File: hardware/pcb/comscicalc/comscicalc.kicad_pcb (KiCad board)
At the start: 2 copper layers, 178.7 x 104.8 mm, 307 parts, among them IC1 TPS92360DCKR, IC2 AP62300TWU-7, IC3 FT811Q-T, IC4 TCA8418RTWR, J1 USB4110-GF-A, J2 TC2050-IDC, J3 4-1734839-0, SW1 SSSS211603, SW10 SW_Push, SW11 SW_Push, SW12 SW_Push, SW13 SW_Push, SW14 SW_Push, SW15 SW_Push, SW16 SW_Push, SW17 SW_Push, SW18 SW_Push, SW19 SW_Push, SW2 SW_Push, SW20 SW_Push, SW21 SW_Push, SW22 SW_Push, SW23 SW_Push, SW24 SW_Push, SW25 SW_Push, SW26 SW_Push, SW27 SW_Push, SW28 SW_Push, SW29 SW_Push, SW3 SW_Push, SW30 SW_Push, SW31 SW_Push, SW32 SW_Push, SW33 SW_Push, SW34 SW_Push, SW35 SW_Push, SW36 SW_Push, SW4 SW_Push, SW5 SW_Push, SW6 SW_Push, SW7 SW_Push, SW8 SW_Push, SW9 SW_Push, U1 USBLC6-2SC6, U2 TM4C1290NCPDTI3R, U3 IS31FL3729-QFLS4-TR, Y1 NX3225GA-25.000M-STD-CRG-2, Y2 DNM, Y3 X1G004171001800

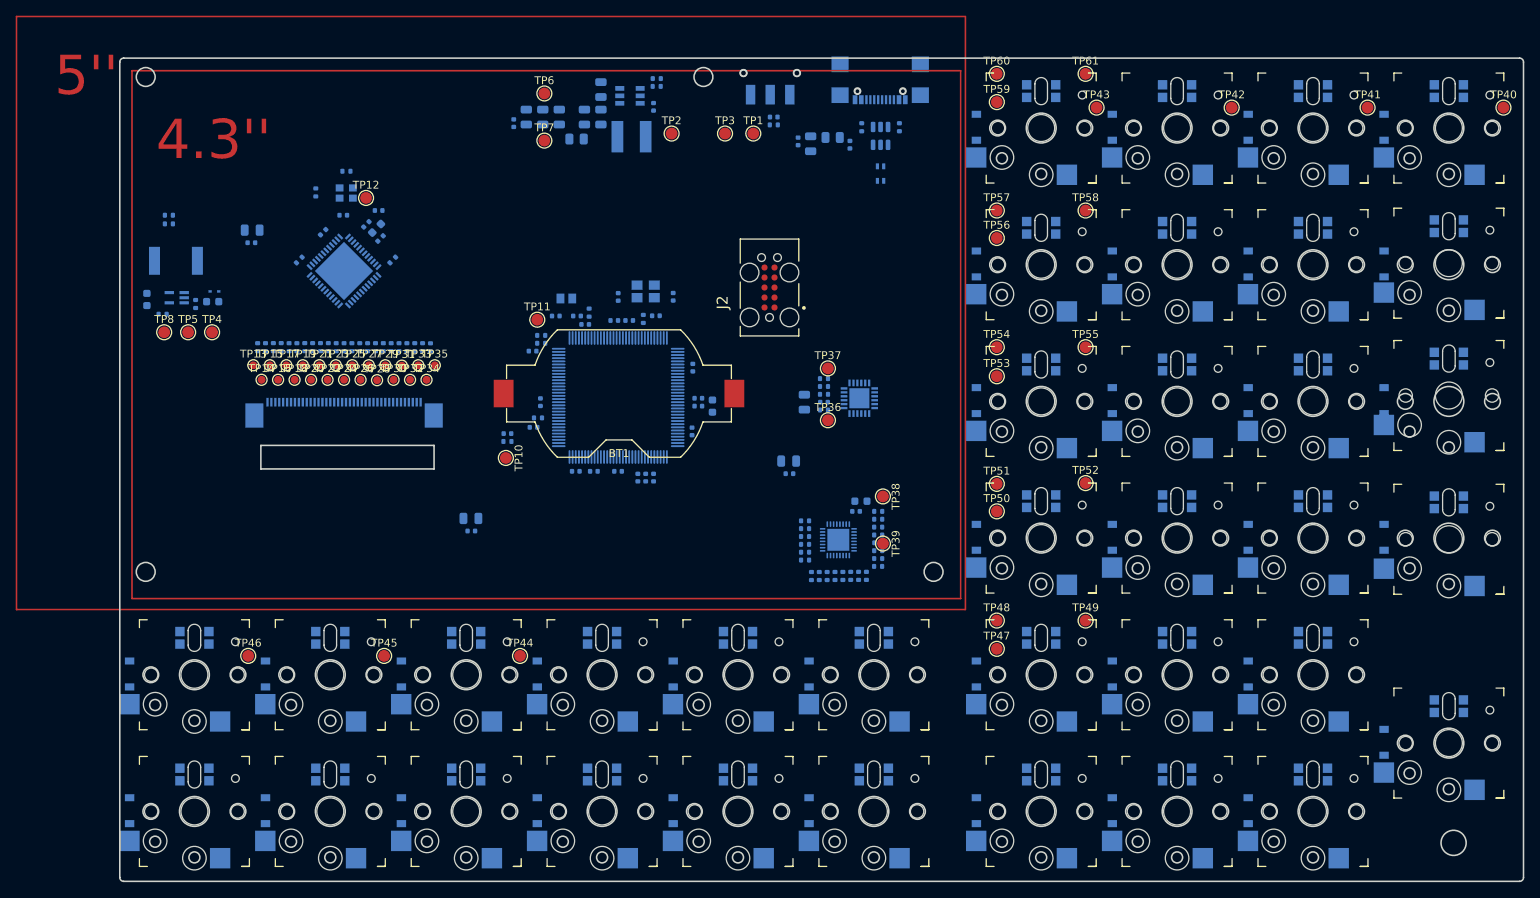
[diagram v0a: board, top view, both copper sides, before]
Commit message: Added a submodule for a display driver that looks nice
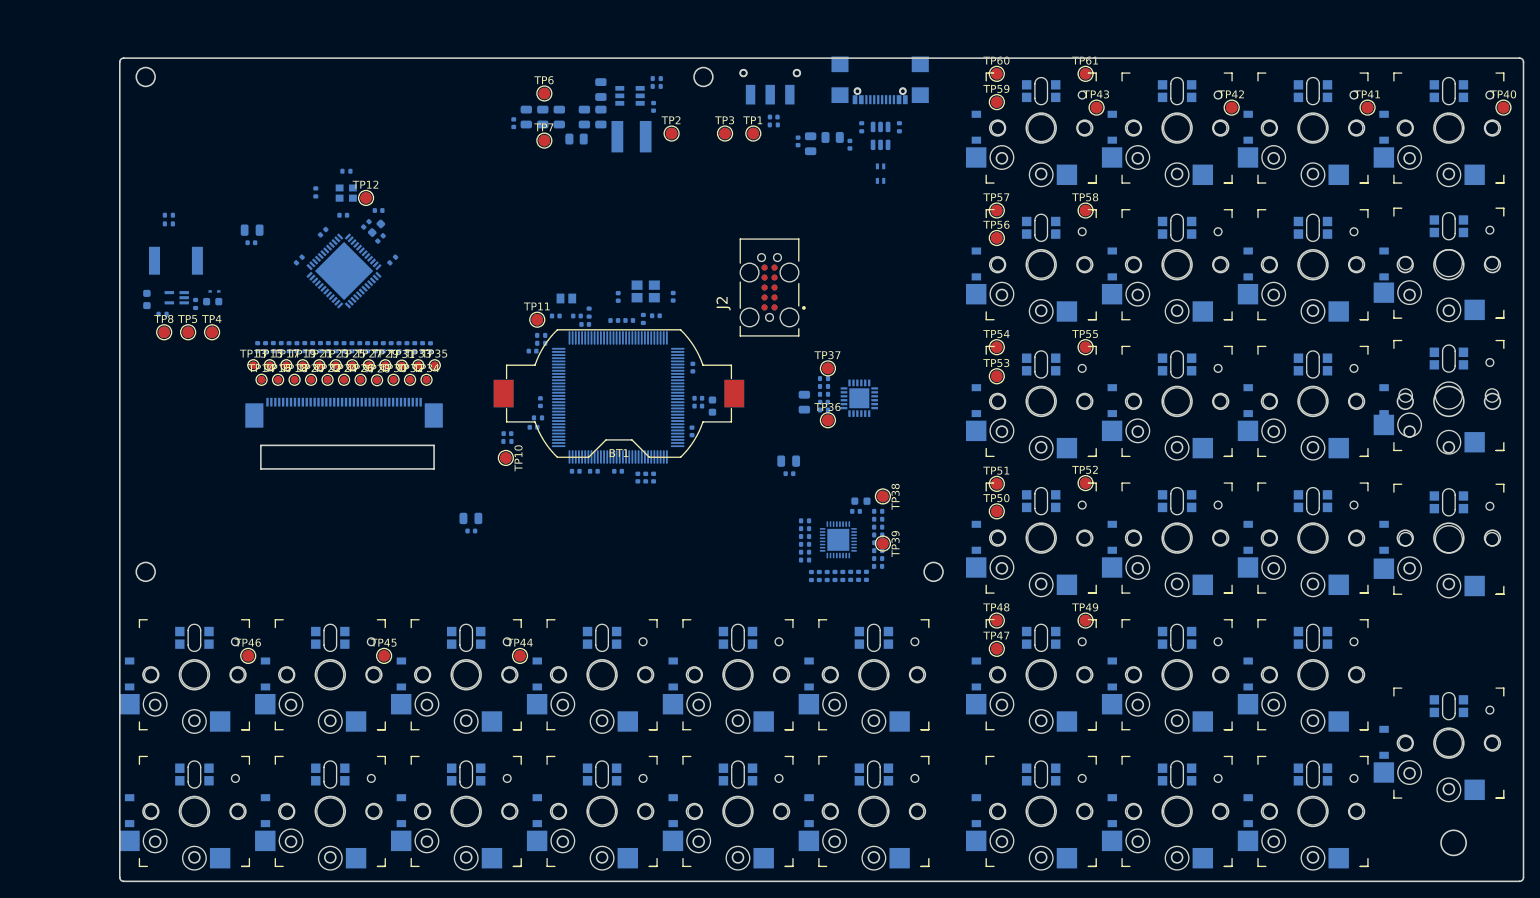
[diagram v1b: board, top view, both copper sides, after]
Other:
- board text removed: "4.3''"
- board text removed: "5''"
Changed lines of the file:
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@@
     )
   )
-  (gr_rect (start 47.7 110.3) (end 168.5 34.8) (layer "F.Cu") (width 0.2) (fill none))
-  (gr_rect (start 62.4 108.9) (end 167.9 41.7) (layer "F.Cu") (width 0.2) (fill none))
   (gr_circle locked (center 65.35 122.45) (end 66.05 122.45) (layer "Edge.Cuts") (width 0.2) (fill none))
   (gr_circle locked (center 178.15 54.85) (end 178.85 54.85) (layer "Edge.Cuts") (width 0.2) (fill none))
@@
   (gr_line locked (start 78.81 89.4) (end 100.86 89.4) (layer "Edge.Cuts") (width 0.2))
   (gr_circle locked (center 207.2 136) (end 208.2 136) (layer "Edge.Cuts") (width 0.2) (fill none))
-  (gr_text "4.3''" (at 72.8 50.5) (layer "F.Cu")
-    (effects (font (size 5 5) (thickness 1)))
-  )
-  (gr_text "5''" (at 56.6 42.35) (layer "F.Cu")
-    (effects (font (size 5 5) (thickness 1)))
-  )
   (group "" (id 36a0b721-c905-4320-b4bf-cef1c2531742)
     (members
@@
     )
   )
-  (group "" (id 875a4b31-1c56-4e62-8e00-f4140add34df)
-    (members
-      2e7074a9-8f71-4208-a054-057960b9fd5e
-      db5af982-772e-4d1b-85a9-7918ce199a17
-    )
-  )
-  (group "" (id d0364e9f-4e64-4d3a-aa0a-40593faaf727)
-    (members
-      5265b37f-07e3-467f-b19c-5eb6ca78b78c
-      9f0c4e08-aefa-45f8-b780-d3d3f61b6f32
-    )
-  )
